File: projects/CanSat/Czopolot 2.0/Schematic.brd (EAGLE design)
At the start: 56.5 x 25 mm, 94 parts

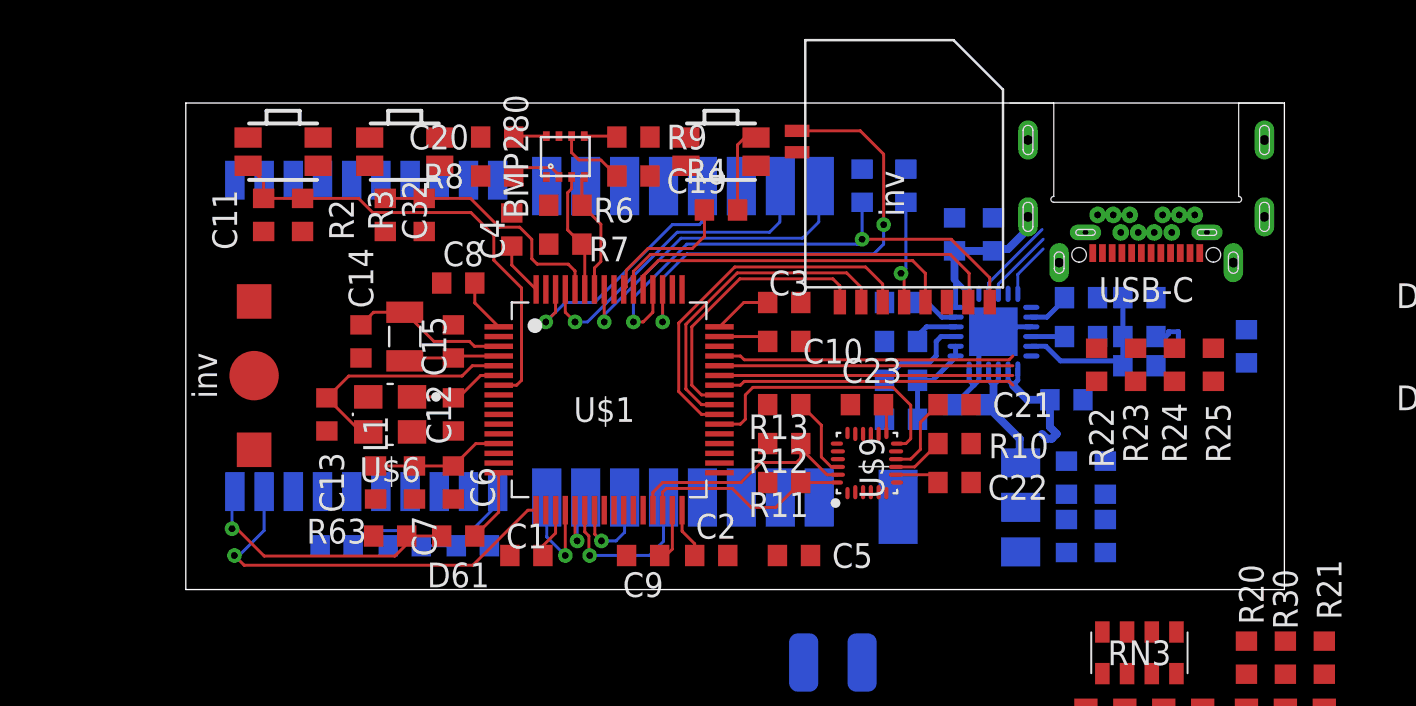
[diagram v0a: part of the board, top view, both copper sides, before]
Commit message: Proposed routing ver.2
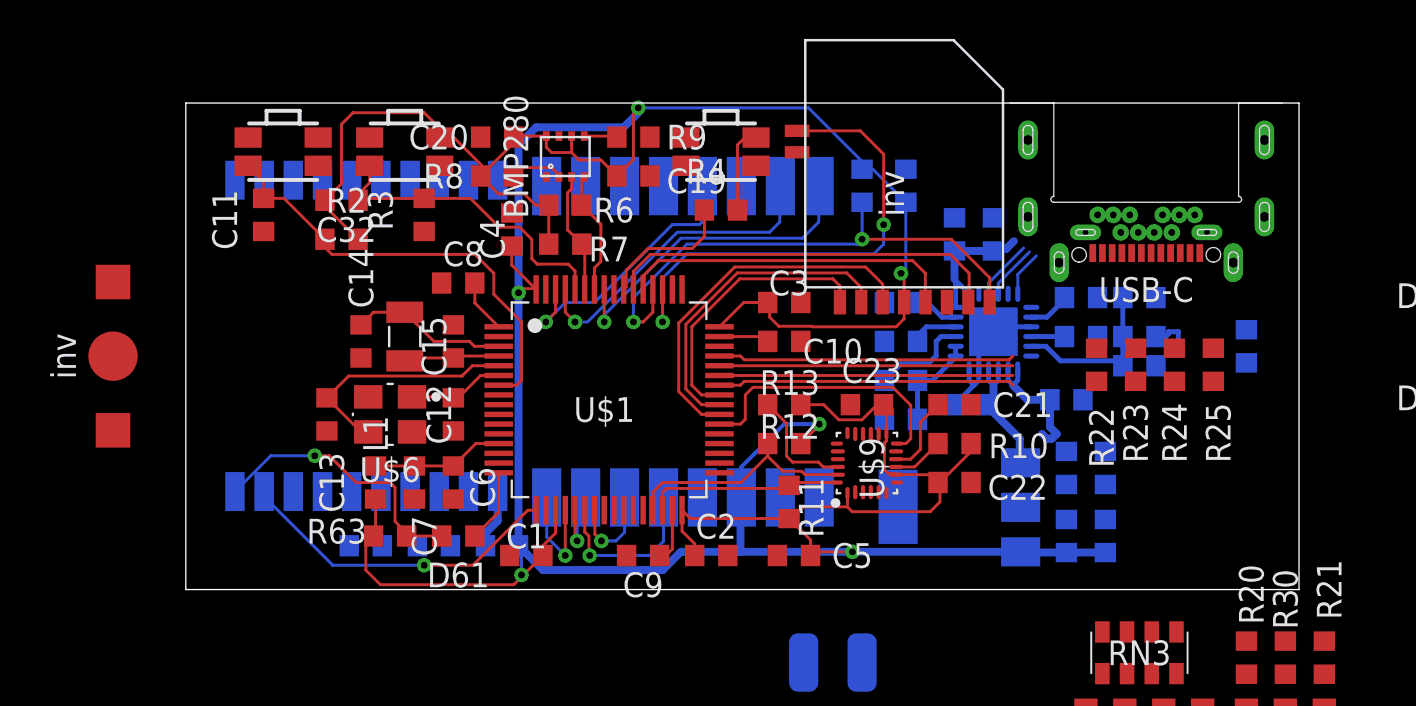
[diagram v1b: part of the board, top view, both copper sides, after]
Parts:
- moved B6 7.32 mm to (-3.74, 12.0)
- moved F61 5.00 mm to (16.2, 2.25), turned to 0 degrees
- moved C32 2.37 mm to (8.00, 20.0), turned to 0 degrees
- moved R2 2.36 mm to (8.00, 18.0), turned to 0 degrees
- moved C61 2.00 mm to (12.8, 2.25), turned to 0 degrees
- moved C62 1.50 mm to (9.25, 2.25)
- moved R11 1.03 mm to (31.0, 4.50), turned to 270 degrees
- moved C28 0.50 mm to (47.2, 6.25)
- moved C29 0.50 mm to (45.2, 6.25)
- turned R12 to 0 degrees
- turned R13 to 0 degrees
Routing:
- net VCC: track 25.5 -> 199.5 mm, vias 1 -> 6
- net N$17: track 9.75 -> 3.04 mm
- net GPS_TX: track 20.9 -> 16.9 mm
- net N$10: track 12.8 -> 16.3 mm
- net MPU_NCS: track 4.19 -> 6.25 mm
- net USB_D+: track 4.44 -> 3.10 mm
- net USB_VBUS: track 8.65 -> 7.35 mm
- net USB_D-: track 3.76 -> 2.82 mm
- net N$7: track 23.9 -> 23.0 mm
- net MPU_SDA: track 10.9 -> 10.1 mm
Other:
- board size 56.5 x 25 mm -> 57.2 x 25 mm

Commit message: Jeezz it's tiny...
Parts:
- moved B6 38.3 mm to (30.5, -5.26), turned to 180 degrees
- moved D6 31.3 mm to (15.0, -7.50)
- moved D7 31.3 mm to (17.0, -7.50)
- moved D8 31.3 mm to (19.0, -7.50)
- moved D9 31.3 mm to (21.0, -7.50)
- moved RN3 31.3 mm to (17.8, -3.50)
- moved B2 30.1 mm to (60.8, 8.50)
- moved B3 30.1 mm to (60.8, 4.00)
- moved R1 27.3 mm to (34.0, 48.0), flipped to the top
- moved C18 27.3 mm to (36.8, 48.0), flipped to the top
- moved C62 26.0 mm to (34.5, 8.50), turned to 270 degrees
- moved C61 22.0 mm to (34.5, 5.50), turned to 270 degrees
- moved C5 21.6 mm to (10.0, -2.25)
- moved U$2 20.5 mm to (36.7, 38.6), turned to 270 degrees
- moved F61 20.5 mm to (34.5, 11.5), turned to 270 degrees
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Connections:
- net N$10: now also BTN_DFU.P$3; no longer BTN_DFU.P$2
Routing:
- net VCC: track 199.5 -> 78.0 mm, vias 6 -> 0
- net GPS_TX: track 16.9 -> 0.00 mm, vias 1 -> 0
- net SD_SW: track 25.6 -> 10.7 mm
- net N$18: track 14.3 -> 0.00 mm, vias 1 -> 0
- net N$6: track 27.7 -> 14.5 mm
- net MPU_INT: track 14.3 -> 3.66 mm
- net N$5: track 21.2 -> 11.6 mm
- net LR_NSS: track 5.71 -> 14.5 mm
- net N$35: track 15.2 -> 6.52 mm
- net N$38: track 15.2 -> 6.61 mm
- net N$25: track 15.1 -> 6.64 mm
- net LR_DIO1: track 16.9 -> 8.46 mm
- net N$37: track 15.1 -> 6.72 mm
- net LR_SCK: track 4.04 -> 12.2 mm
- net LR_BUSY: track 16.4 -> 8.50 mm
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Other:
- board size 57.2 x 25 mm -> 36.2 x 25.5 mm

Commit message: Work work...
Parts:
- added R14: 7k, Unified:R0603
- added R26: 11k, Unified:R0603
- added R27: 12k, Unified:R0603
- moved D9 41.2 mm to (14.8, 33.2), turned to 0 degrees
- moved D6 41.2 mm to (20.8, 33.2), turned to 0 degrees
- moved D8 40.8 mm to (16.8, 33.2), turned to 0 degrees
- moved D7 40.8 mm to (18.8, 33.2), turned to 0 degrees
- moved RN3 32.8 mm to (18.0, 29.2), turned to 180 degrees
- moved R63 26.0 mm to (-1.00, -22.5), turned to 0 degrees
- moved D61 22.0 mm to (-1.00, -17.5)
- moved R3 4.91 mm to (7.75, 20.2), turned to 180 degrees
- moved L1 4.50 mm to (6.50, 6.00)
- moved C32 3.50 mm to (11.2, 20.2)
- moved C20 3.09 mm to (14.5, 23.0), turned to 270 degrees
- moved C6 2.25 mm to (4.25, 6.00)
- moved C7 2.25 mm to (2.00, 6.00)
- moved BTN_DFU 1.75 mm to (8.75, 23.0)
- moved BTN_RST 1.75 mm to (3.50, 23.0)
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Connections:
- new net N$21: R26.1, R27.2
- net B+: now also R14.2
- net GND: now also BTN_RST.P$1, BTN_USR.P$1, BTN_USR.P$4, R27.1; no longer BTN_USR.P$2, R19.2
- net GPS_RX: now also U$1.37, U$3.P$10; no longer D61.2, U$1.16
- net GPS_TX: now also U$1.38; no longer U$1.17
- net MPU_INT: now also U$1.36; no longer U$1.38
- net N$10: now also BTN_DFU.P$2
- net N$16: now also BTN_USR.P$2, BTN_USR.P$3; no longer BTN_USR.P$4
- net N$18: now also R14.1, R26.2; no longer D61.1, R63.1, U$3.P$10
- net N$29: no longer R19.1
- net N$7: now also BTN_RST.P$3
- net VCC: now also BTN_DFU.P$1; no longer R63.2
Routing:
- net GND: track 10.6 -> 100.8 mm
- net N$10: track 9.46 -> 17.8 mm, vias 0 -> 2
- net GPS_TX: track 0.00 -> 8.20 mm, vias 0 -> 1
- net N$29: track 8.78 -> 5.43 mm
- net VCC: track 78.0 -> 81.3 mm
- net GPS_RX: track 3.97 -> 6.67 mm, vias 0 -> 1
- net N$16: track 5.12 -> 2.57 mm
- net BMP_SDI: track 3.01 -> 5.14 mm
- net BMP_SDA: track 6.74 -> 8.55 mm
- net MPU_INT: track 3.66 -> 5.35 mm
- net N$13: track 8.61 -> 7.18 mm
- net N$7: track 18.3 -> 16.9 mm
- net BMP_SCL: track 8.79 -> 9.86 mm
- net MPU_SDA: track 14.3 -> 15.3 mm
- net MPU_SCL: track 13.3 -> 14.3 mm
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
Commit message: Work work
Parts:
- removed RN3: 560R, resistor-dil:EXBS8V
- added R28, R29: ?10k, Unified:R0603
- added R31, R33: 100k, Unified:R0603
- added RN1: (no value), resistor-dil:EXBV8V
- added U$14, U$15: NMOSFET, SobieskiSat2:INV_SOT-89
- moved D6 36.0 mm to (-2.75, 6.00)
- moved D7 35.7 mm to (-4.25, 6.00)
- moved D8 35.3 mm to (-5.75, 6.00)
- moved D9 35.0 mm to (-7.25, 6.00)
- moved R14 30.8 mm to (17.0, -2.50)
- moved R26 30.8 mm to (17.0, -6.00)
- moved R27 30.8 mm to (17.0, -9.50)
- moved U$13 30.0 mm to (61.8, -9.40), turned to 90 degrees
- moved D5 27.2 mm to (59.5, -9.40), turned to 90 degrees
- moved R1 24.3 mm to (45.8, 26.8), turned to 0 degrees
- moved D4 18.4 mm to (59.6, -3.95), turned to 90 degrees
- moved R63 17.8 mm to (2.50, -5.00)
- moved D61 14.9 mm to (2.50, -3.00)
- moved C18 14.2 mm to (34.2, 34.0)
- moved U$12 13.6 mm to (61.6, -3.70), turned to 90 degrees
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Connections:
- net N$4 renamed SD_CLK
- removed net N$39: D4.2, U$12.P$2
- removed net N$40: D5.2, U$13.P$2
- removed net N$46: RN3.7, U$1.49
- removed net N$47: RN3.8, U$1.46
- removed net N$48: RN3.6, U$1.50
- removed net N$5: U$1.54, U$2.P$7
- removed net N$6: R1.2, U$1.52, U$2.P$8
- new net IN_MOT1: R28.2, U$14.1
- new net IN_MOT2: R29.2, U$15.1
- new net N$41: D5.1, U$13.P$1, U$15.2, U$15.2@1
- new net N$42: D4.1, U$12.P$1, U$14.2, U$14.2@1
- new net SD_CMD: U$1.54, U$2.P$3
- new net SD_D0: U$1.39, U$2.P$7
- new net SD_D1: U$1.40, U$2.P$8
- new net SD_D2: U$1.51, U$2.P$1
- new net SD_D3: R1.2, U$1.52, U$2.P$2
- net GND: now also R28.1, R29.1, U$14.3, U$15.3; no longer D4.1, D5.1, U$12.P$1, U$13.P$1
- net N$1: now also RN1.8; no longer U$1.39, U$2.P$3
- net N$2: now also RN1.6; no longer U$1.40, U$2.P$2
- net N$3: now also RN1.7; no longer U$1.41, U$2.P$1
- net N$43: now also RN1.1; no longer RN3.1
- net N$44: now also RN1.2; no longer RN3.2
- net N$45: now also RN1.3; no longer RN3.3
- net N$49: now also RN1.4; no longer RN3.4
- net N$50: now also RN1.5; no longer RN3.5, U$1.56
- net SD_SW: now also U$1.41; no longer U$1.51
- net VCC: now also R31.1, R33.1
- net VIN: now also D4.2, D5.2, U$12.P$2, U$13.P$2
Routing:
- net SD_D0: track 0.00 -> 16.9 mm
- net SD_D1: track 0.00 -> 15.9 mm
- net N$1: track 15.6 -> 0.00 mm
- net N$6: track 14.7 -> 0.00 mm, vias 2 -> 0
- net N$2: track 14.5 -> 0.00 mm
- net SD_D2: track 0.00 -> 13.5 mm, vias 0 -> 2
- net N$3: track 13.4 -> 0.00 mm
- net SD_CMD: track 0.00 -> 13.1 mm
- net SD_D3: track 0.00 -> 12.6 mm, vias 0 -> 2
- net N$5: track 11.8 -> 0.00 mm
- net N$10: track 17.8 -> 22.4 mm
- net SD_SW: track 11.2 -> 15.8 mm
- net LR_NSS: track 14.6 -> 16.4 mm
- net LR_SCK: track 12.6 -> 14.4 mm
- net GPS_RX: track 6.67 -> 4.89 mm
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
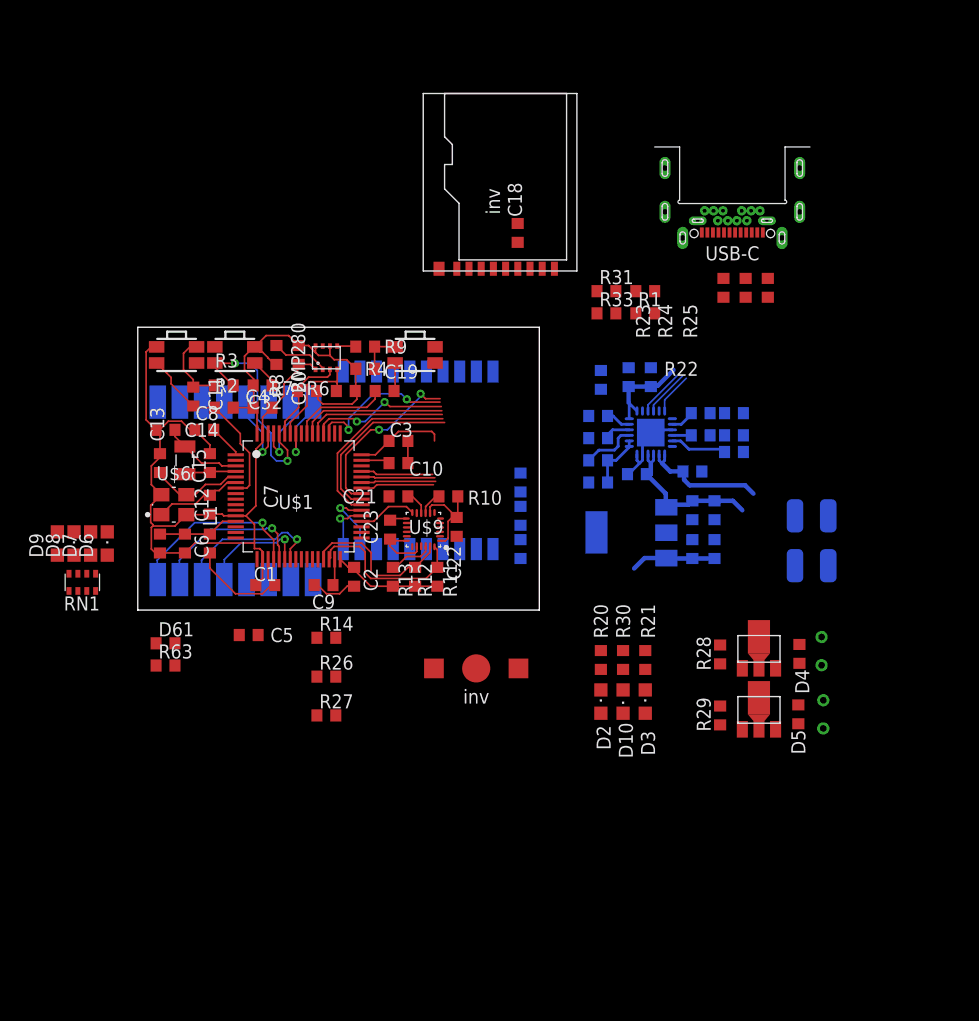
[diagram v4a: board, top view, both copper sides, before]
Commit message: Schematic changes
BQ25606 replaced with 24270
USB OTG replaced with USB
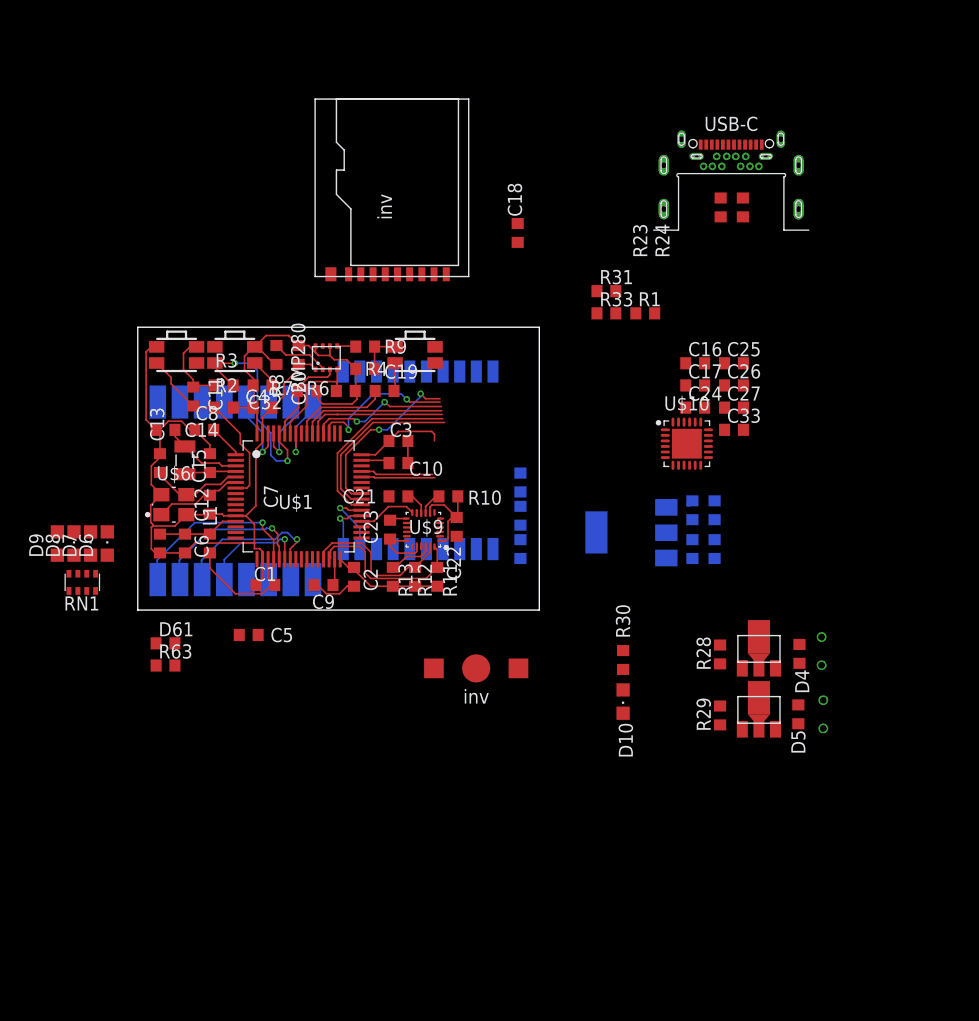
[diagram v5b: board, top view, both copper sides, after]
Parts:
- removed B2, B3: (no value), SobieskiSat2:CON_BATTERY
- removed D1: ZENER, Unified:R0603
- removed D2, D3: LED0805, Unified:CHIPLED_0805
- removed L2: 1uH, Unified:R0603
- removed R14: 7k, Unified:R0603
- removed R15, R19: 10k, Unified:R0603
- removed R16: 240R, Unified:R0603
- removed R17: 30.1k, Unified:R0603
- removed R18: 5.23k, Unified:R0603
- removed R20, R21: 2.2k, Unified:R0603
- removed R22, R25: 560R, Unified:R0603
- removed R26: 11k, Unified:R0603
- removed R27: 12k, Unified:R0603
- removed R5: 450R, Unified:R0603
- added C33: (no value), Unified:C0603
- C16, C24, C27: value 10u -> (none)
- C17: value 1u -> (none)
- C25: value 4.7u -> (none)
- C26: value 47n -> (none)
- U$10: value BQ25606 -> BQ24270; device SobieskiSat2:QFN50P400X400X100-25T250N -> SobieskiSat2:QFN50P400X400X100-25T270N
- moved C25 14.0 mm to (53.8, 22.2), flipped to the top
- moved C26 14.0 mm to (53.8, 20.2), flipped to the top, turned to 0 degrees
- moved C27 10.6 mm to (53.8, 18.2), flipped to the top, turned to 0 degrees
- moved C16 9.96 mm to (50.2, 22.2), flipped to the top, turned to 0 degrees
- moved U$2 9.76 mm to (22.9, 34.1)
- moved R23 7.25 mm to (52.5, 36.3)
- moved R24 7.25 mm to (54.5, 36.3)
- moved C17 6.05 mm to (50.2, 20.2), flipped to the top, turned to 0 degrees
- moved C24 5.76 mm to (50.2, 18.2), flipped to the top, turned to 0 degrees
- moved U$7 4.00 mm to (53.5, 40.0), turned to 0 degrees
- moved U$10 3.40 mm to (49.5, 15.0), flipped to the top, turned to 0 degrees
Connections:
- removed net ?BQ_VSET: U$10.12
- removed net ?HOST_OTG: U$10.6
- removed net B+: B2.P$1, B3.P$1, C24.1, R14.2, U$10.13, U$10.14
- removed net N$18: R14.1, R26.2
- removed net N$20: C16.2, U$10.23
- removed net N$21: R26.1, R27.2
- removed net N$22: C26.2, L2.1, U$10.19, U$10.20
- removed net N$24: R5.2, U$10.10
- removed net N$26: C25.1, R18.1, U$10.22
- removed net N$27: R16.2, U$10.8
- removed net N$28: C26.1, U$10.21
- removed net N$29: R17.2, R18.2, U$10.11
- removed net N$30: D2.C, R20.2
- removed net N$31: D3.C, R21.2
- removed net N$32: R20.1, U$10.7
- removed net N$33: R21.1, U$10.5
- removed net N$36: R15.2
- removed net N$38: R25.1, U$1.42
- removed net USB_ID: R22.2
- new net N$4: U$1.42
- net GND: now also U$7.A$1, U$7.A$12, U$7.B$1, U$7.B$12; no longer B2.P$2, B3.P$2, C16.1, C17.1, C24.2, C25.2, C27.1, D1.1, R15.1, R16.1, R17.1, R27.1, R5.1, U$10.17, U$10.18, U$10.25, U$10.9
- net N$37: no longer R22.1
- net USB_D+: now also U$7.A$6, U$7.B$7; no longer U$10.3
- net USB_D-: now also U$7.A$7, U$7.B$6; no longer U$10.4
- net USB_VBUS: now also U$7.A$4, U$7.A$9, U$7.B$4, U$7.B$9; no longer C17.2, D1.2, R25.2, U$10.1, U$10.24
- net VIN: no longer C27.2, D2.A, D3.A, L2.2, U$10.15, U$10.16
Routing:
- net VIN: track 14.4 -> 0.78 mm
- net B+: track 11.6 -> 0.00 mm
- net USB_VBUS: track 8.77 -> 0.00 mm
- net GND: track 100.8 -> 93.1 mm
- net VCC: track 81.6 -> 74.0 mm
- net N$37: track 6.72 -> 0.00 mm
- net N$38: track 6.61 -> 0.00 mm
- net N$29: track 5.43 -> 0.00 mm
- net N$28: track 5.02 -> 0.00 mm
- net N$22: track 5.01 -> 0.00 mm
- net USB_D+: track 4.52 -> 0.00 mm
- net USB_D-: track 4.23 -> 0.00 mm
- net ?HOST_OTG: track 3.77 -> 0.00 mm
- net N$26: track 2.44 -> 0.00 mm
- net N$20: track 2.27 -> 0.00 mm
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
